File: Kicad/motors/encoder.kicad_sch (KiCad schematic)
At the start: 30 parts, among them IC301 SN74LVC2G17, IC302 SN74LVC2G17, IC303 OPB610, IC304 OPB610, IC305 OPB610, IC306 OPB610, IC307 LM3480-33, K301 Front, K302 Rear, Q301 BC846B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

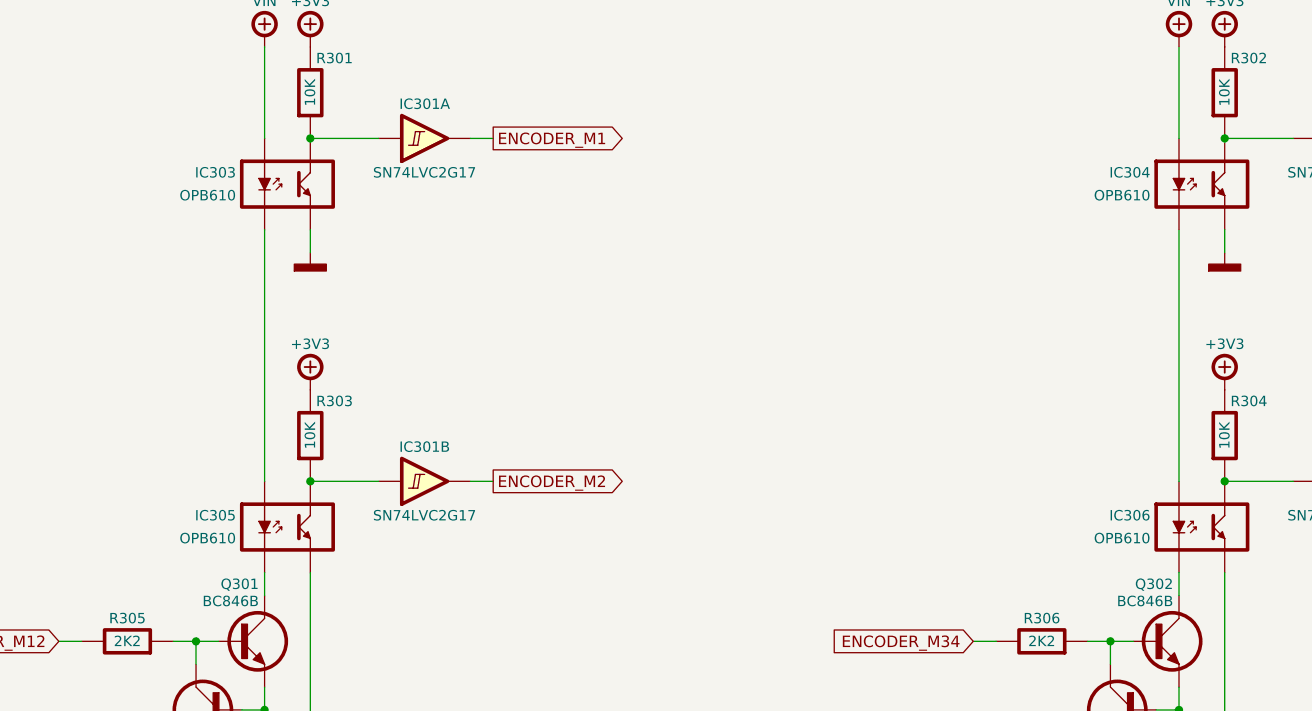
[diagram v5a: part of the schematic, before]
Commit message: Update Motors
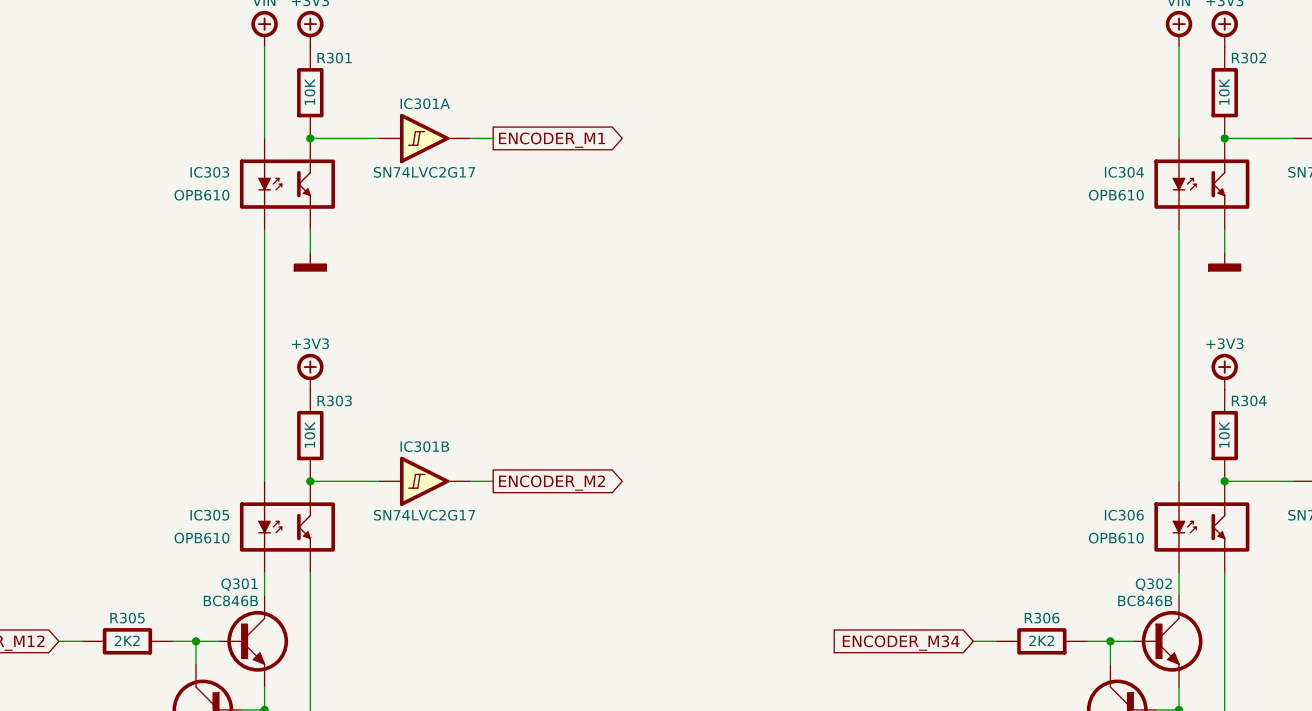
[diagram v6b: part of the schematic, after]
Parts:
- IC303, IC304, IC305, IC306: value OPB610 -> TTE-OPB610; MOUSER 828-OPB610 -> (none); Mouser (none) -> 828-OPB610; Name (none) -> OPB610
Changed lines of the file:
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@@
   (symbol (lib_id "tronixio:TTE-OPB610") (at 195.58 91.44 0) (unit 1)
     (in_bom yes) (on_board yes)
-    (property "Reference" "IC306" (id 0) (at 189.865 90.17 0)
-      (effects (font (size 1.15 1.15)) (justify right))
-    )
-    (property "Value" "OPB610" (id 1) (at 189.865 92.71 0)
-      (effects (font (size 1.15 1.15)) (justify right))
-    )
-    (property "Footprint" "tronixio:zzzOPB-610" (id 2) (at 195.58 104.14 0)
-      (effects (font (size 1 1)) hide)
-    )
-    (property "Datasheet" "https://www.ttelectronics.com/products/categories/optoelectronics/optoelectronics/opb610/" (id 3) (at 195.58 104.14 0)
-      (effects (font (size 1 1)) hide)
-    )
-    (property "MOUSER" "828-OPB610" (id 4) (at 195.58 106.68 0)
-      (effects (font (size 1 1)) hide)
+    (property "Reference" "IC306" (id 0) (at 189.23 90.17 0)
+      (effects (font (size 1.15 1.15)) (justify right))
+    )
+    (property "Value" "TTE-OPB610" (id 1) (at 195.58 104.14 0)
+      (effects (font (size 1.15 1.15)) hide)
+    )
+    (property "Footprint" "tronixio:zzzOPB-610" (id 2) (at 195.58 106.68 0)
+      (effects (font (size 1 1)) hide)
+    )
+    (property "Datasheet" "https://www.ttelectronics.com/products/categories/optoelectronics/optoelectronics/opb610/" (id 3) (at 195.58 109.22 0)
+      (effects (font (size 1 1)) hide)
+    )
+    (property "Mouser" "828-OPB610" (id 4) (at 195.58 111.76 0)
+      (effects (font (size 1 1)) hide)
+    )
+    (property "Name" "OPB610" (id 5) (at 189.23 92.71 0)
+      (effects (font (size 1.15 1.15)) (justify right))
     )
     (pin "1")
@@
   (symbol (lib_id "tronixio:TTE-OPB610") (at 93.98 53.34 0) (unit 1)
     (in_bom yes) (on_board yes)
-    (property "Reference" "IC303" (id 0) (at 88.265 52.07 0)
-      (effects (font (size 1.15 1.15)) (justify right))
-    )
-    (property "Value" "OPB610" (id 1) (at 88.265 54.61 0)
-      (effects (font (size 1.15 1.15)) (justify right))
-    )
-    (property "Footprint" "tronixio:zzzOPB-610" (id 2) (at 93.98 66.04 0)
-      (effects (font (size 1 1)) hide)
-    )
-    (property "Datasheet" "https://www.ttelectronics.com/products/categories/optoelectronics/optoelectronics/opb610/" (id 3) (at 93.98 66.04 0)
-      (effects (font (size 1 1)) hide)
-    )
-    (property "MOUSER" "828-OPB610" (id 4) (at 93.98 68.58 0)
-      (effects (font (size 1 1)) hide)
+    (property "Reference" "IC303" (id 0) (at 87.63 52.07 0)
+      (effects (font (size 1.15 1.15)) (justify right))
+    )
+    (property "Value" "TTE-OPB610" (id 1) (at 93.98 66.04 0)
+      (effects (font (size 1.15 1.15)) hide)
+    )
+    (property "Footprint" "tronixio:zzzOPB-610" (id 2) (at 93.98 68.58 0)
+      (effects (font (size 1 1)) hide)
+    )
+    (property "Datasheet" "https://www.ttelectronics.com/products/categories/optoelectronics/optoelectronics/opb610/" (id 3) (at 93.98 71.12 0)
+      (effects (font (size 1 1)) hide)
+    )
+    (property "Mouser" "828-OPB610" (id 4) (at 93.98 73.66 0)
+      (effects (font (size 1 1)) hide)
+    )
+    (property "Name" "OPB610" (id 5) (at 87.63 54.61 0)
+      (effects (font (size 1.15 1.15)) (justify right))
     )
     (pin "1")
@@
   (symbol (lib_id "tronixio:TTE-OPB610") (at 93.98 91.44 0) (unit 1)
     (in_bom yes) (on_board yes)
-    (property "Reference" "IC305" (id 0) (at 88.265 90.17 0)
-      (effects (font (size 1.15 1.15)) (justify right))
-    )
-    (property "Value" "OPB610" (id 1) (at 88.265 92.71 0)
-      (effects (font (size 1.15 1.15)) (justify right))
-    )
-    (property "Footprint" "tronixio:zzzOPB-610" (id 2) (at 93.98 104.14 0)
-      (effects (font (size 1 1)) hide)
-    )
-    (property "Datasheet" "https://www.ttelectronics.com/products/categories/optoelectronics/optoelectronics/opb610/" (id 3) (at 93.98 104.14 0)
-      (effects (font (size 1 1)) hide)
-    )
-    (property "MOUSER" "828-OPB610" (id 4) (at 93.98 106.68 0)
-      (effects (font (size 1 1)) hide)
+    (property "Reference" "IC305" (id 0) (at 87.63 90.17 0)
+      (effects (font (size 1.15 1.15)) (justify right))
+    )
+    (property "Value" "TTE-OPB610" (id 1) (at 93.98 104.14 0)
+      (effects (font (size 1.15 1.15)) hide)
+    )
+    (property "Footprint" "tronixio:zzzOPB-610" (id 2) (at 93.98 106.68 0)
+      (effects (font (size 1 1)) hide)
+    )
+    (property "Datasheet" "https://www.ttelectronics.com/products/categories/optoelectronics/optoelectronics/opb610/" (id 3) (at 93.98 109.22 0)
+      (effects (font (size 1 1)) hide)
+    )
+    (property "Mouser" "828-OPB610" (id 4) (at 93.98 111.76 0)
+      (effects (font (size 1 1)) hide)
+    )
+    (property "Name" "OPB610" (id 5) (at 87.63 92.71 0)
+      (effects (font (size 1.15 1.15)) (justify right))
     )
     (pin "1")
@@
   (symbol (lib_id "tronixio:TTE-OPB610") (at 195.58 53.34 0) (unit 1)
     (in_bom yes) (on_board yes)
-    (property "Reference" "IC304" (id 0) (at 189.865 52.07 0)
-      (effects (font (size 1.15 1.15)) (justify right))
-    )
-    (property "Value" "OPB610" (id 1) (at 189.865 54.61 0)
-      (effects (font (size 1.15 1.15)) (justify right))
-    )
-    (property "Footprint" "tronixio:zzzOPB-610" (id 2) (at 195.58 66.04 0)
-      (effects (font (size 1 1)) hide)
-    )
-    (property "Datasheet" "https://www.ttelectronics.com/products/categories/optoelectronics/optoelectronics/opb610/" (id 3) (at 195.58 66.04 0)
-      (effects (font (size 1 1)) hide)
-    )
-    (property "MOUSER" "828-OPB610" (id 4) (at 195.58 68.58 0)
-      (effects (font (size 1 1)) hide)
-    )
-    (pin "1")
+    (property "Reference" "IC304" (id 0) (at 189.23 52.07 0)
+      (effects (font (size 1.15 1.15)) (justify right))
+    )
+    (property "Value" "TTE-OPB610" (id 1) (at 195.58 66.04 0)
+      (effects (font (size 1.15 1.15)) hide)
+    )
+    (property "Footprint" "tronixio:zzzOPB-610" (id 2) (at 195.58 68.58 0)
+      (effects (font (size 1 1)) hide)
+    )
+    (property "Datasheet" "https://www.ttelectronics.com/products/categories/optoelectronics/optoelectronics/opb610/" (id 3) (at 195.58 71.12 0)
+      (effects (font (size 1 1)) hide)
+    )
+    (property "Mouser" "828-OPB610" (id 4) (at 195.58 73.66 0)
+      (effects (font (size 1 1)) hide)
+    )
+    (property "Name" "OPB610" (id 5) (at 189.23 54.61 0)
+      (effects (font (size 1.15 1.15)) (justify right))
+    )
+    (pin "1")

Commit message: Update Motor
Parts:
- removed Q301, Q302, Q303, Q304: BC846B, tronixio:SOT-23-3, symbol tronixio:BC846BLT1G-SOT-23
- added Q301, Q302: NEXPERIA-BC846BS, symbol tronixio:NEXPERIA-BC846BS
- IC301, IC302: symbol tronixio:SN74LVC2G17-SOT -> tronixio:TI-SN74LVC2G17-SOT; MOUSER 595-SN74LVC2G17DBVR -> (none); Mouser (none) -> 595-SN74LVC2G17DBVR; Name (none) -> SN74LVC2G17
- IC303, IC304, IC305, IC306: footprint tronixio:zzzOPB-610 -> (none)
- IC307: value LM3480-33 -> (none); symbol tronixio:LM3480-33-SOT -> tronixio:TI-LM3480-33-SOT; MOUSER 926-LM3480IM33.3NOPB -> (none); Mouser (none) -> 926-LM3480IM33.3NOPB; Name (none) -> LM3480-33
- K301, K302: footprint tronixio:zzHARWIN-M20-782104x -> (none); MOUSER 855-M20-782104 -> (none); Mouser (none) -> 855-M20-782104
- LED301: MOUSER 604-APT3216LSECKJ3RV -> (none); Mouser (none) -> 604-APT3216LSECKJ3RV
- TP301: footprint tronixio:zzzHARWIN-S1751 -> (none); MOUSER 855-S1751-46 -> (none); Mouser (none) -> 855-S1751-46
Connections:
- net GND: now also Q301.4 (E), Q302.4 (E)
- net at R308.1: now also Q302.1 (E), Q302.5 (B)
- net at R306.2: now also Q302.2 (B), Q302.3 (C)
- net at R307.1: now also Q301.1 (E), Q301.5 (B)
- net at R305.2: now also Q301.2 (B), Q301.3 (C)
- net at IC305.2 (CATHODE): now also Q301.6 (C)
- net at IC306.2 (CATHODE): now also Q302.6 (C)

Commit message: Update
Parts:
- IC303, IC304, IC305, IC306: footprint (none) -> tronixio:zzzOPB-610
- IC307: value (none) -> LM3480-33
- K301, K302: footprint (none) -> tronixio:zzHARWIN-M20-782104x
- LED301: value +3V3 -> LED-1206-RED; Name (none) -> Red
- Q301, Q302: footprint (none) -> tronixio:zzzSOT-70-6
- TP301: footprint (none) -> tronixio:HARWIN-S1751; Name (none) -> GND
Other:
- moved on the sheet: K301, K302
